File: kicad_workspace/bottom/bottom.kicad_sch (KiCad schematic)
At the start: 26 parts, among them M1 N20_MOTOR_EXTENDED_SHAFT, M2 N20_MOTOR_EXTENDED_SHAFT, U1 DRV8833PWP, U2 ULTRASOUND_T_R, U3 ATmega4809-A, U4 BNO055, Y1 32.768kHz

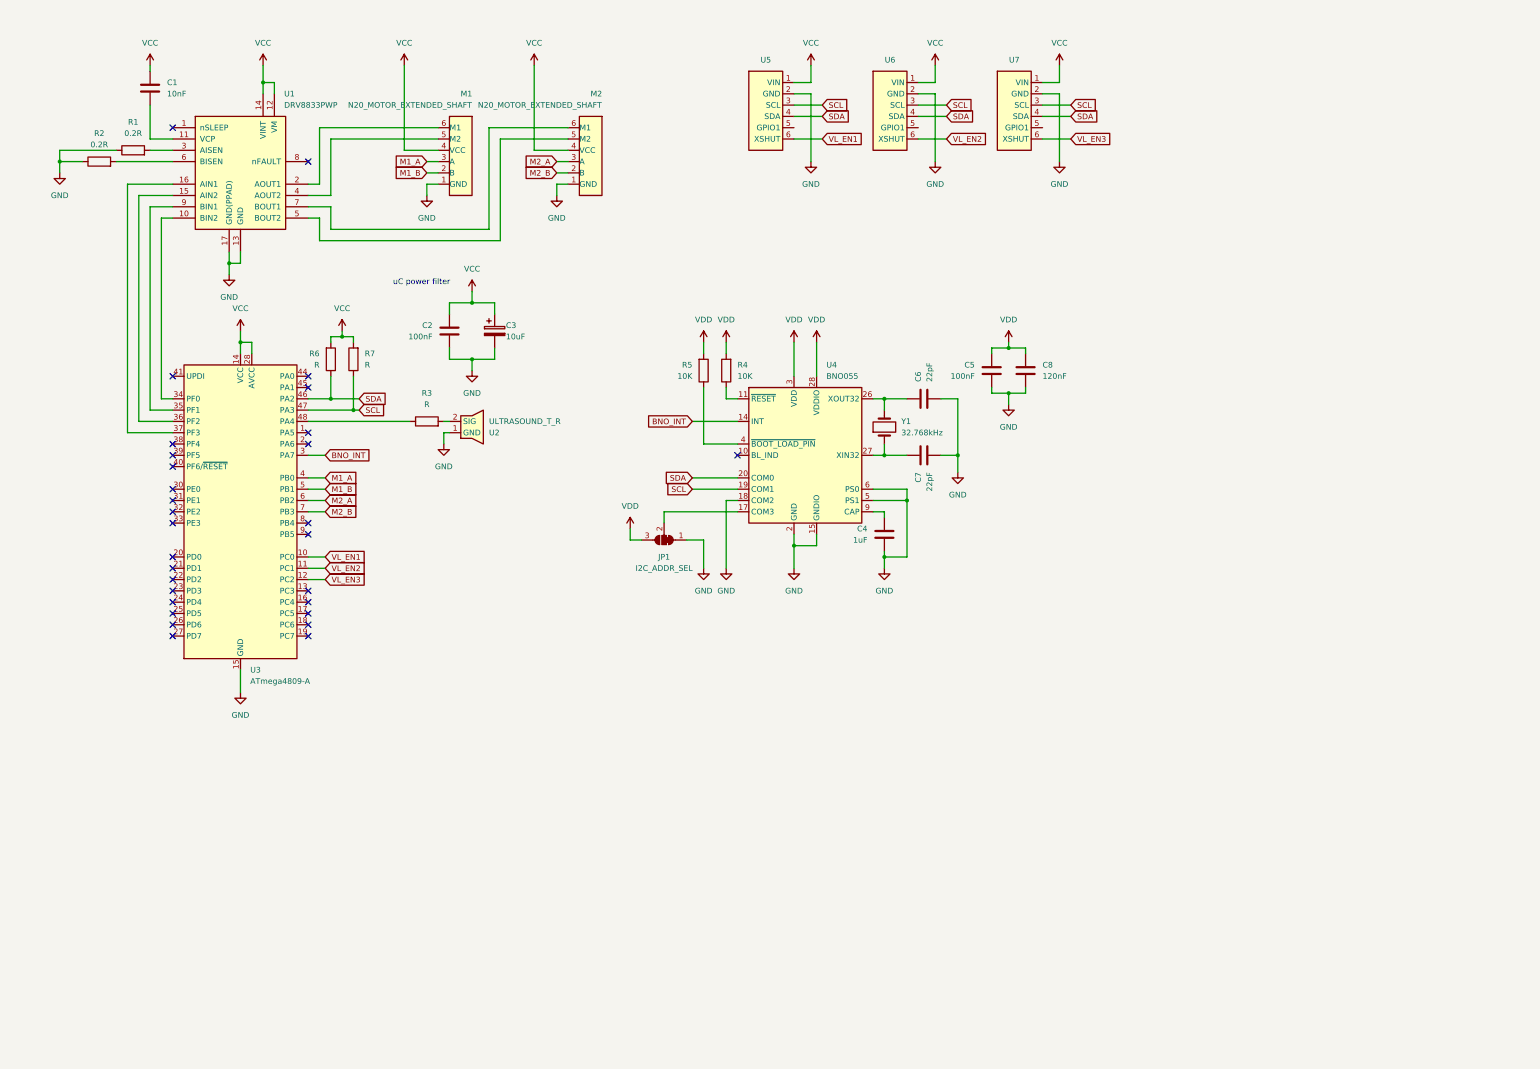
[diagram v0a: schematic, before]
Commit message: change vcc and vdd symbols. add routes for bno055 sensor on pcb
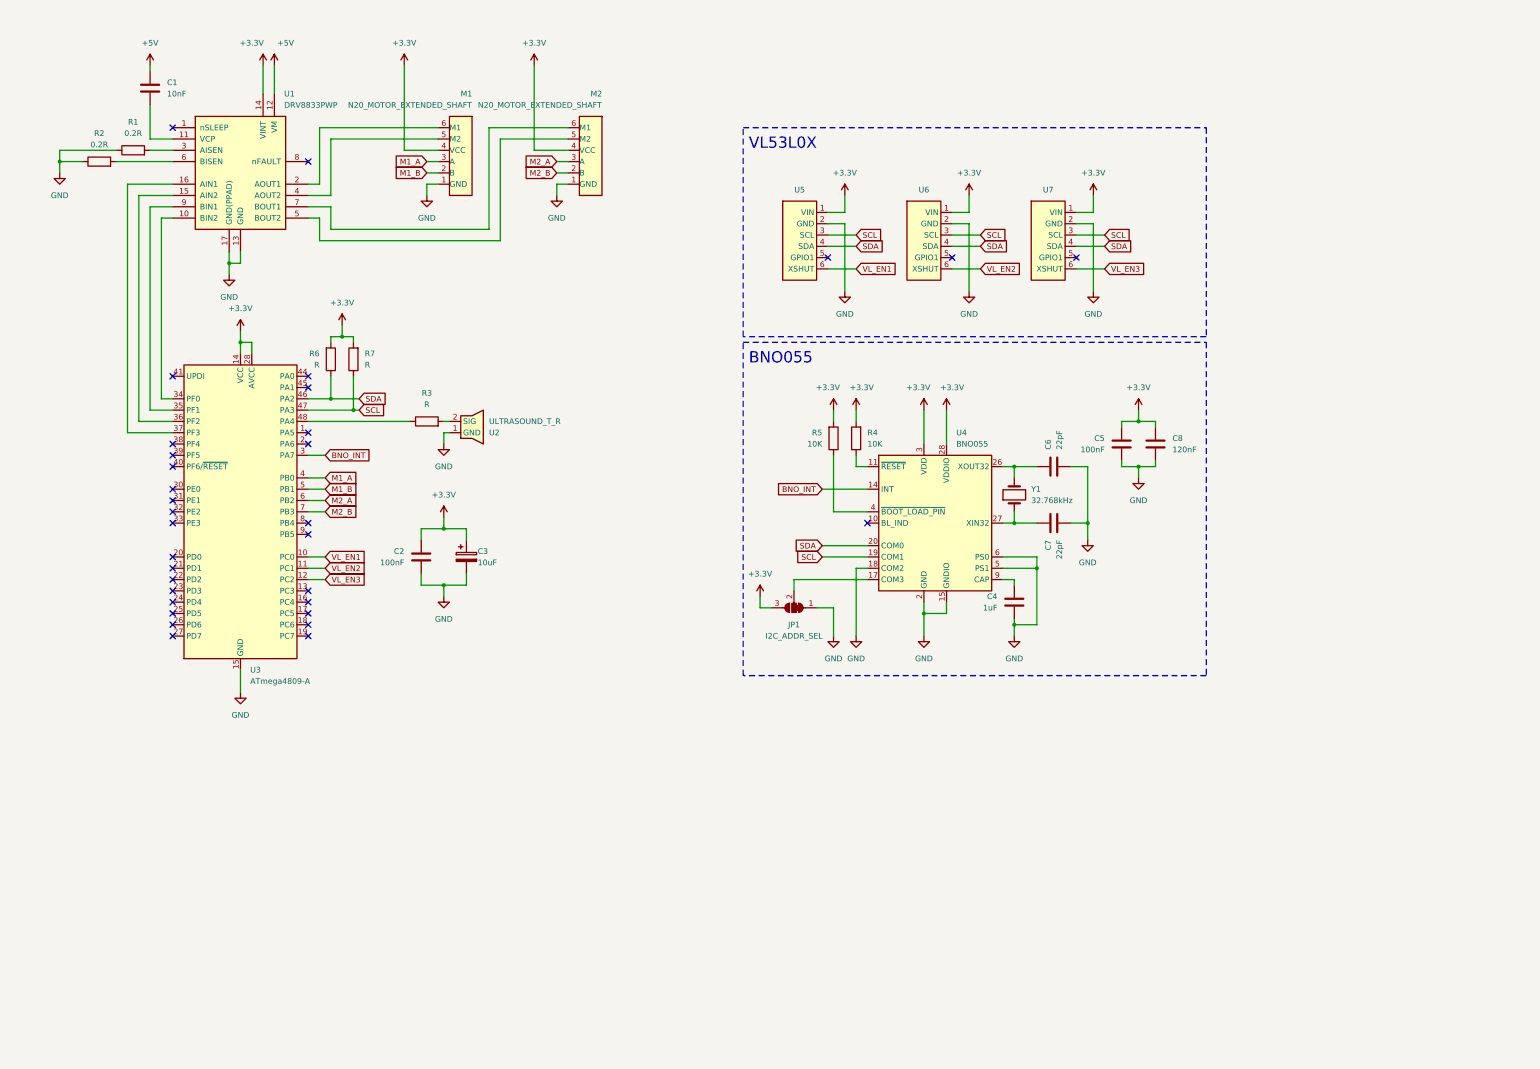
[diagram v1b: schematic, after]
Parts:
- C1, C2, C4, C5, C6, C7, C8: footprint (none) -> Capacitor_SMD:C_0805_2012Metric
- C3: footprint (none) -> Capacitor_SMD:CP_Elec_4x3
- R1, R2, R3, R4, R5, R6, R7: footprint (none) -> Resistor_SMD:R_0805_2012Metric
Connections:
- net VDD is gone; now on net +3.3V: C5.1, C8.1, JP1.3 (B), R4.2, R5.2, U4.28 (VDDIO), U4.3 (VDD)
- net VCC renamed +3.3V
- net +3.3V: no longer C1.1, U1.12 (VM)
- new net +5V: C1.1, U1.12 (VM)
- no-connect marks 30 -> 33
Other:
- note added: "BNO055"
- note added: "VL53L0X"
- note removed: "uC power filter"
- moved on the sheet: C2, C3, C4, C5, C6, C7, C8, JP1, R4, R5, U4, U5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

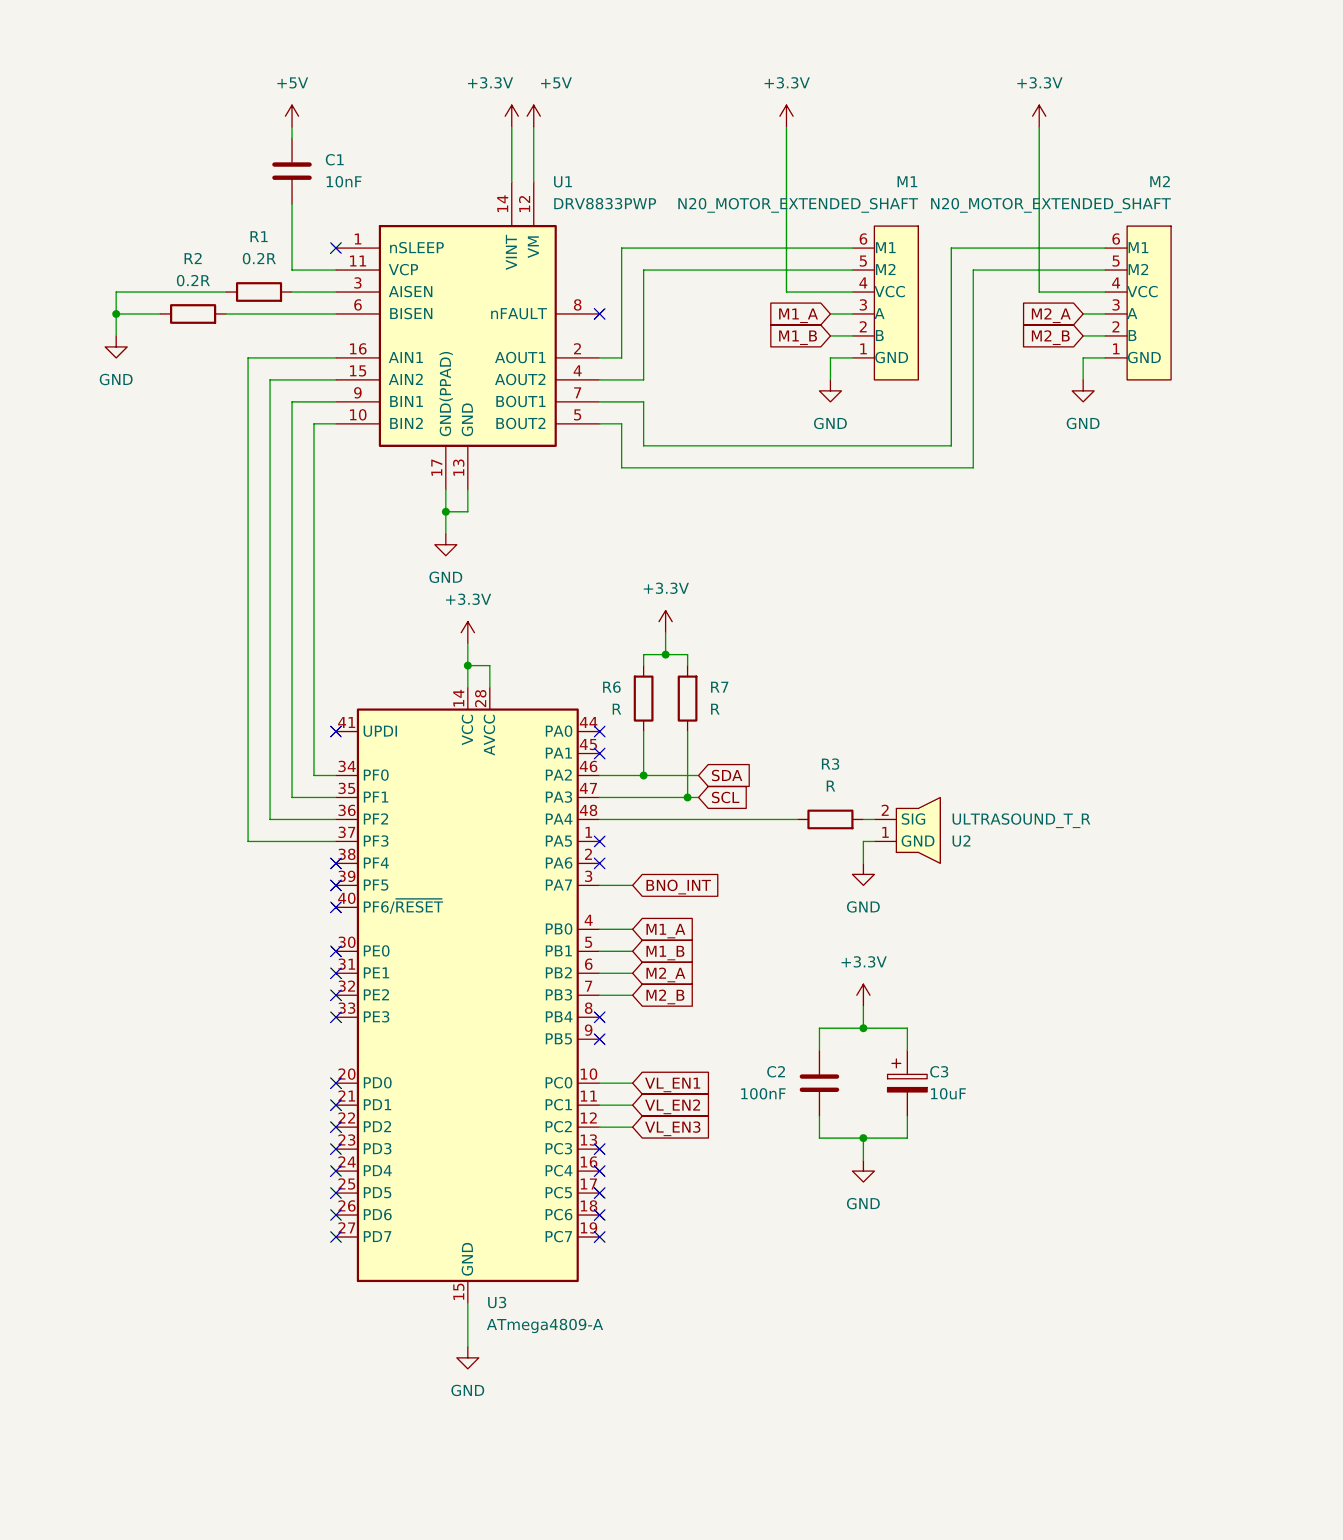
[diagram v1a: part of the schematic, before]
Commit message: divided drv8833 and uC to separate sections
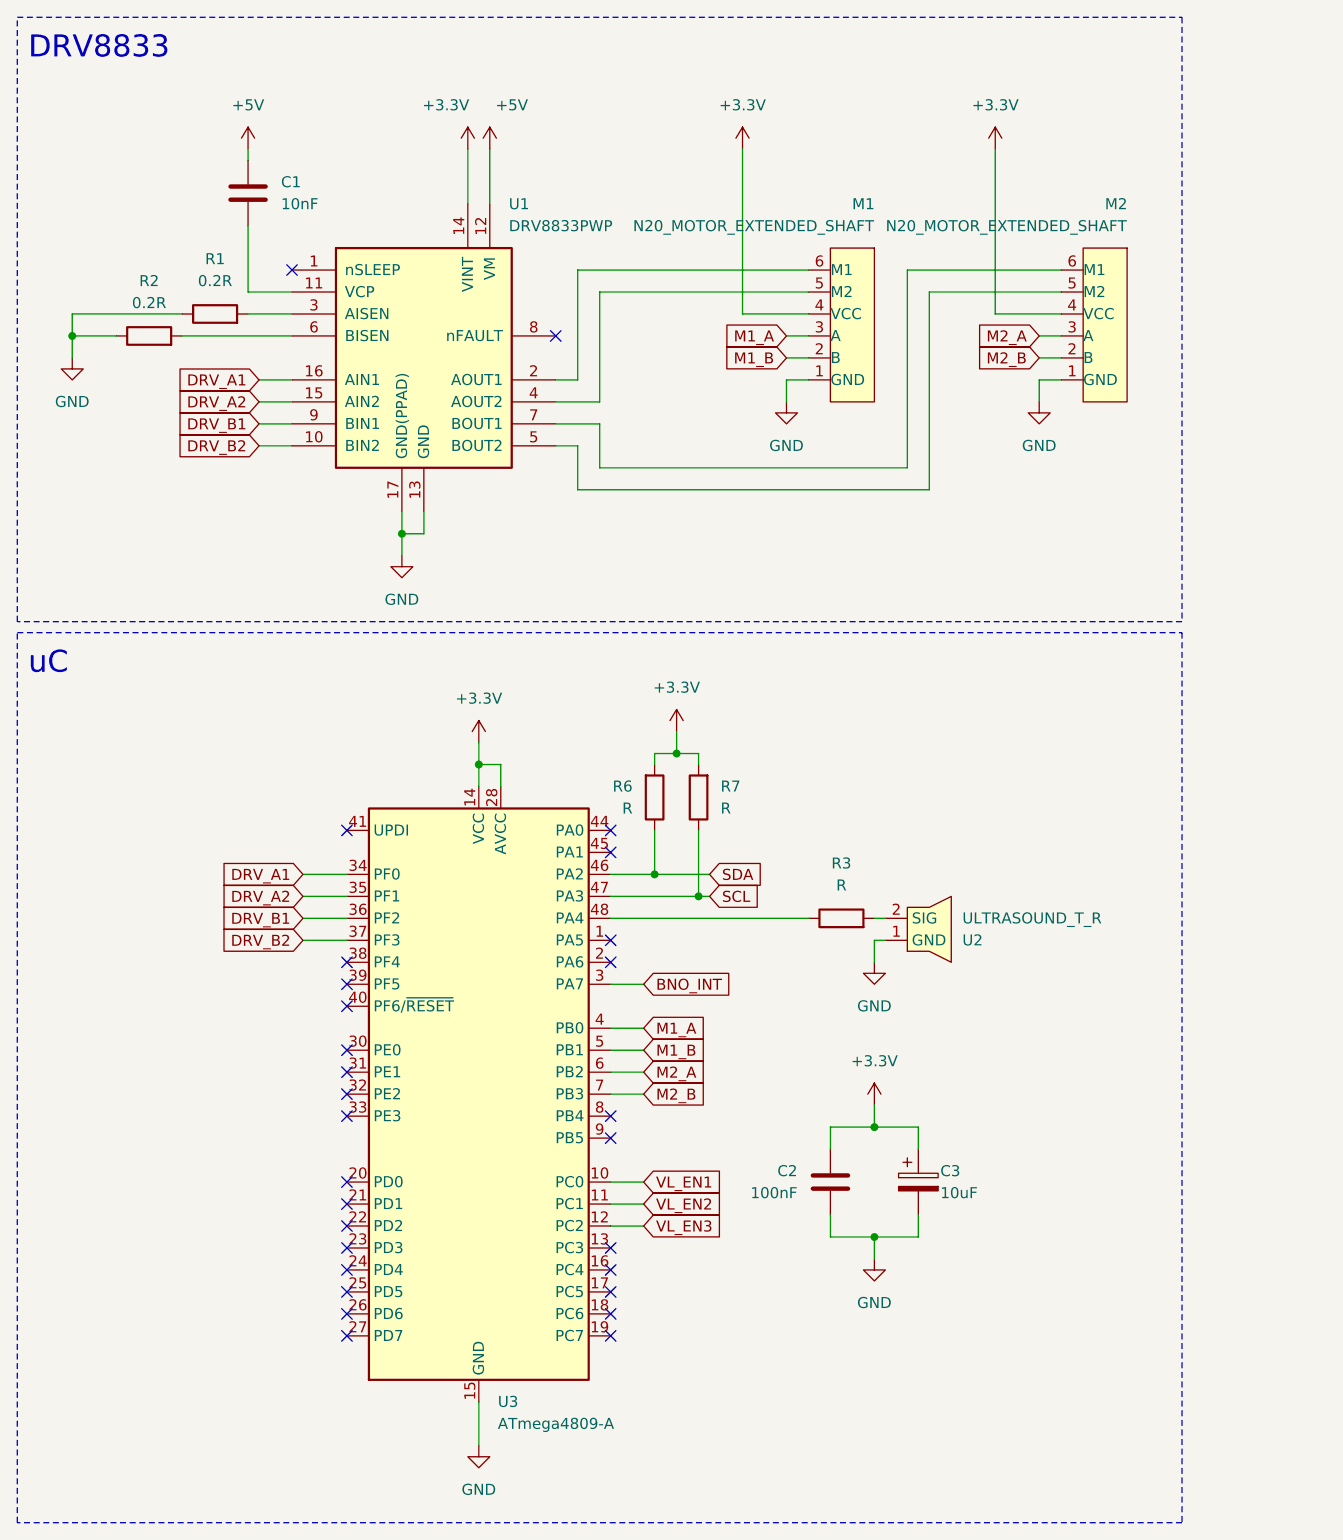
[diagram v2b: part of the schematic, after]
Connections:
- net DRV_A1: now reaches U3.34 (PF0)
- net DRV_A1: now also U1.16 (AIN1); no longer U1.10 (BIN2)
- net DRV_A2: now reaches U1.15 (AIN2)
- net DRV_A2: now also U3.35 (PF1); no longer U3.36 (PF2)
- net DRV_B2: now reaches U3.37 (PF3)
- net DRV_B2: now also U1.10 (BIN2); no longer U1.16 (AIN1)
- net DRV_B1: now reaches U1.9 (BIN1)
- net DRV_B1: now also U3.36 (PF2); no longer U3.35 (PF1)
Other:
- note added: "DRV8833"
- note added: "uC"
- moved on the sheet: C1, C2, C3, M1, M2, R1, R2, R3, R6, R7, U1, U2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

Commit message: add battery connector
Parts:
- added J1: Battery connector, Connector_JST:JST_XH_B2B-XH-AM_1x02_P2.50mm_Vertical, symbol Connector_Generic:Conn_01x02
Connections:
- net GND: now also J1.2 (Pin_2)
- new net VCC: J1.1 (Pin_1)
